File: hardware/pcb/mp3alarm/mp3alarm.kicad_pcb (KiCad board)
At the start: 2 copper layers, 68.6 x 47 mm, 18 parts, among them J1 AUDIO, J2 SW0, J3 SW1, J4 SW2, J5 I2C, J6 TM1637, J7 microSD, J9 ANT, U1 UDA1334A_Breakout, U2 mini_esp32, U3 RDA5807

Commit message: Updated PCB (added QR code, OSHW logo, etc) Some bugfixes for webinterface Updated README
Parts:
- added G***: LOGO, qr-code:qr-code, B.Cu at (98.8, 95.5)
- added G***: LOGO, qr-code:oshw, B.Cu at (99.1, 75.9)
- added G***: LOGO, qr-code:oshw, F.Cu at (120.1, 79.2)
- added J8: 5V, Connector_PinHeader_2.54mm:PinHeader_1x02_P2.54mm_Vertical, F.Cu at (47.0, 71.6)
- added JTAG: debug, Connector_PinHeader_2.54mm:PinHeader_2x05_P2.54mm_Vertical_SMD, B.Cu at (65.5, 96.3)
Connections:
- U2 pad 13: Net-(U2-Pad13) -> TMS
- U2 pad 18: Net-(U2-Pad18) -> TCK
- U2 pad 28: RDA_L -> I2S_MUTE
- U2 pad 30: Net-(U2-Pad30) -> TDI
- U2 pad 36: I2S_MUTE -> Net-(U2-Pad36)
- U2 pad 37: Net-(U2-Pad37) -> TDO
- U2 pad 4: Net-(U2-Pad4) -> RDA_L
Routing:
- net 5V: track 59.1 -> 95.9 mm
- net TDI: track 0.00 -> 30.1 mm, vias 0 -> 1
- net RDA_L: track 25.8 -> 8.17 mm
- net SD_CMD: track 18.5 -> 34.7 mm, vias 1 -> 2
- net TDO: track 0.00 -> 15.1 mm, vias 0 -> 1
- net TMS: track 0.00 -> 11.6 mm
- net TCK: track 0.00 -> 10.1 mm
- net SD_CD: track 20.3 -> 28.8 mm, vias 1 -> 2
- net I2S_MUTE: track 34.8 -> 27.5 mm, vias 0 -> 2
- net VCC: track 88.1 -> 94.1 mm
- net GND: vias 6 -> 8
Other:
- board text added: "ESP32 alarm clock v0.3"
- board text added: "NC"
- board text added: "TCK"
- board text added: "TDI"
- board text added: "TDO"
- board text added: "TMS"
- board text added: "VCC"
- board text removed: "ESP32 alarm clock"

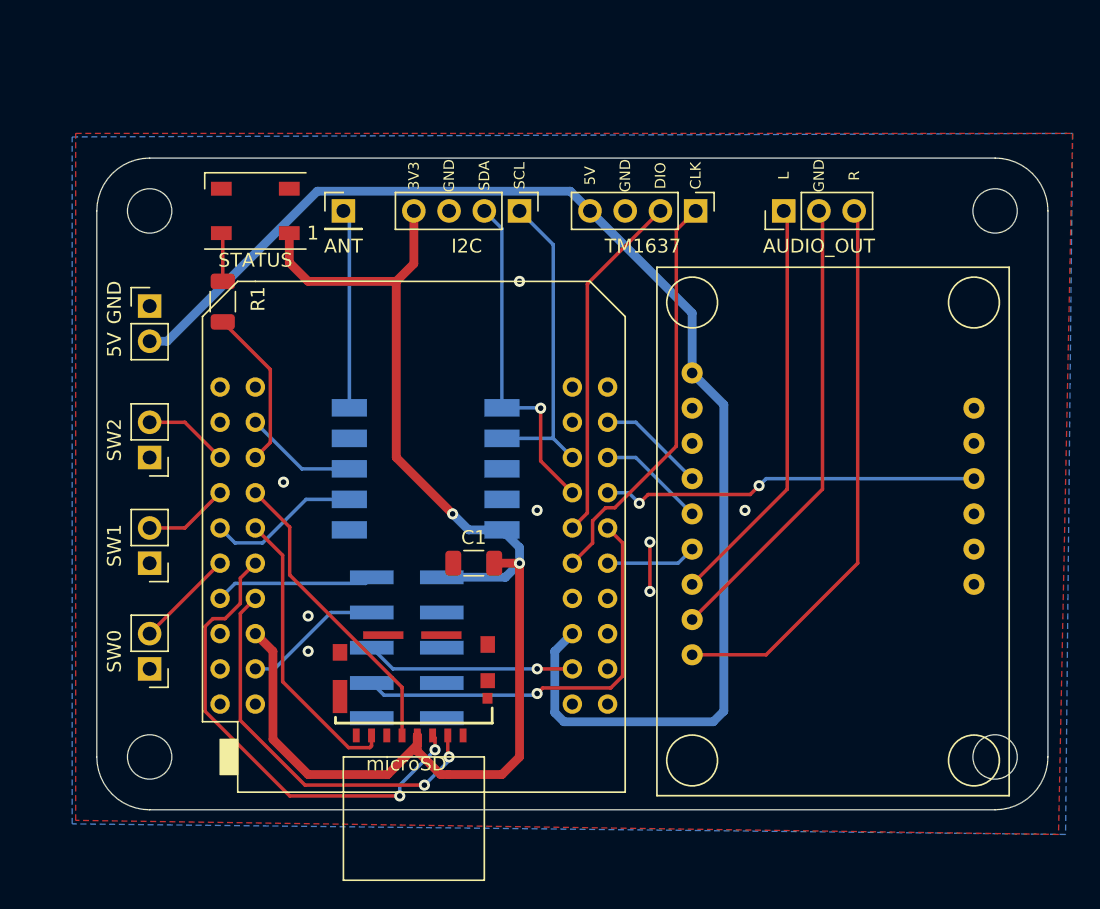
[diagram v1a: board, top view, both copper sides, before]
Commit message: New PCB with RDA5807FP
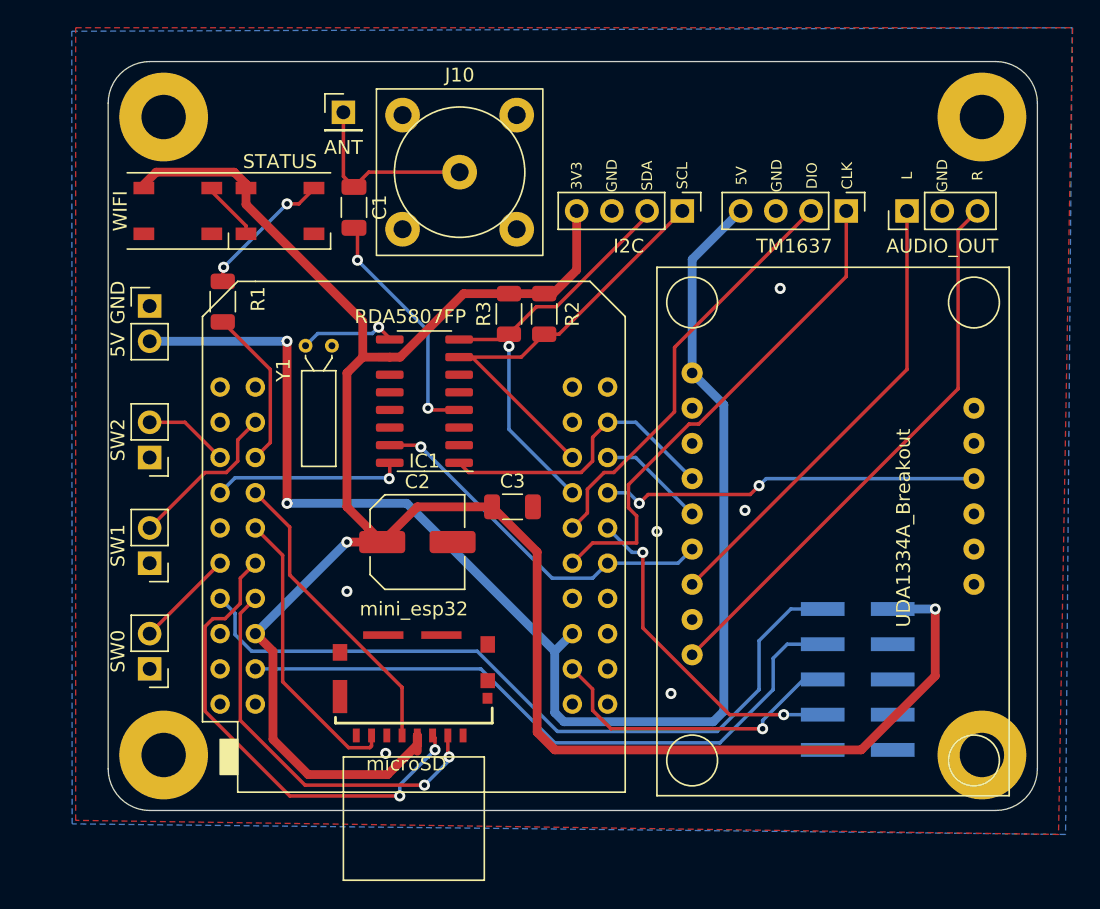
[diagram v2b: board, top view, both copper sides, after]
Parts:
- removed G***: LOGO, qr-code:qr-code
- removed G*** (x2): LOGO, qr-code:oshw
- removed JTAG: debug, Connector_PinHeader_2.54mm:PinHeader_2x05_P2.54mm_Vertical_SMD
- removed REF** (x4): MountingHole_3.2mm_M3, MountingHole:MountingHole_3.2mm_M3
- removed U3: RDA5807, pcb:RDA5807
- added C2: 10uF, Capacitor_SMD:C_Elec_6.3x5.4, F.Cu at (66.3, 88.6)
- added C3: 22nF, Capacitor_SMD:C_1206_3216Metric, F.Cu at (73.2, 86.1)
- added D2: WS2812B, LED_SMD:LED_WS2812B_PLCC4_5.0x5.0mm_P3.2mm, F.Cu at (49.0, 64.8)
- added H1: MountingHole_Pad, MountingHole:MountingHole_3.2mm_M3_Pad, F.Cu at (48.0, 58.0)
- added H2: MountingHole_Pad, MountingHole:MountingHole_3.2mm_M3_Pad, F.Cu at (48.0, 104.0)
- added H3: MountingHole_Pad, MountingHole:MountingHole_3.2mm_M3_Pad, F.Cu at (107.0, 104.0)
- added H4: MountingHole_Pad, MountingHole:MountingHole_3.2mm_M3_Pad, F.Cu at (107.0, 58.0)
- added IC1: RDA5807FP, Package_SO:SOP-16_3.9x9.9mm_P1.27mm, F.Cu at (66.8, 78.5)
- added J0: debug, Connector_PinHeader_2.54mm:PinHeader_2x05_P2.54mm_Vertical_SMD, B.Cu at (98.0, 98.6)
- added J10: Conn_Coaxial, Connector:F_Sat_Connector, F.Cu at (69.3, 62.0)
- added R2: 10k, Resistor_SMD:R_1206_3216Metric, F.Cu at (75.4, 72.2)
- added R3: 10k, Resistor_SMD:R_1206_3216Metric, F.Cu at (72.9, 72.2)
- added Y1: Crystal, Crystal:Crystal_C26-LF_D2.1mm_L6.5mm_Horizontal, F.Cu at (58.2, 74.5)
- C1: value C -> 1nF
- moved C1 27.1 mm to (61.7, 64.5), turned to -90 degrees
- moved J5 11.7 mm to (85.4, 64.8)
- moved J6 10.9 mm to (97.2, 64.8)
- moved J1 8.89 mm to (101.6, 64.8)
- moved J9 7.11 mm to (61.0, 57.7)
- moved D1 1.78 mm to (56.4, 64.8), turned to 0 degrees
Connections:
- C1 pad 1: GND -> ANT
- C1 pad 2: VCC -> Net-(C1-Pad2)
- J7 pad 1: Net-(J7-Pad1) -> unconnected-(J7-Pad1)
- J7 pad 8: Net-(J7-Pad8) -> unconnected-(J7-Pad8)
- J7 pad 9: Net-(J7-Pad9) -> unconnected-(J7-Pad9)
- U1 pad 10: Net-(U1-Pad10) -> unconnected-(U1-Pad10)
- U1 pad 11: Net-(U1-Pad11) -> unconnected-(U1-Pad11)
- U1 pad 13: Net-(U1-Pad13) -> unconnected-(U1-Pad13)
- U1 pad 14: Net-(U1-Pad14) -> unconnected-(U1-Pad14)
- U1 pad 15: Net-(U1-Pad15) -> unconnected-(U1-Pad15)
- U1 pad 2: Net-(U1-Pad2) -> unconnected-(U1-Pad2)
- U2 pad 15: Net-(U2-Pad15) -> unconnected-(U2-Pad15)
- U2 pad 17: Net-(U2-Pad17) -> unconnected-(U2-Pad17)
- U2 pad 19: Net-(U2-Pad19) -> unconnected-(U2-Pad19)
- U2 pad 2: Net-(U2-Pad2) -> unconnected-(U2-Pad2)
- U2 pad 20: Net-(U2-Pad20) -> unconnected-(U2-Pad20)
- U2 pad 21: Net-(U2-Pad21) -> unconnected-(U2-Pad21)
- U2 pad 23: Net-(U2-Pad23) -> unconnected-(U2-Pad23)
- U2 pad 3: Net-(U2-Pad3) -> unconnected-(U2-Pad3)
- U2 pad 34: Net-(U2-Pad34) -> unconnected-(U2-Pad34)
- U2 pad 36: Net-(U2-Pad36) -> unconnected-(U2-Pad36)
- U2 pad 38: Net-(U2-Pad38) -> unconnected-(U2-Pad38)
- U2 pad 39: Net-(U2-Pad39) -> unconnected-(U2-Pad39)
- U2 pad 4: RDA_L -> SW1
- U2 pad 40: Net-(U2-Pad40) -> unconnected-(U2-Pad40)
- U2 pad 7: SW1 -> I2S_RADIO_DOUT
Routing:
- net VCC: track 94.1 -> 161.7 mm
- net TMS: track 11.6 -> 54.0 mm
- net TCK: track 10.1 -> 47.4 mm
- net GND: track 36.9 -> 0.00 mm, vias 8 -> 6
- net I2S_BCLK: track 6.52 -> 26.6 mm, vias 0 -> 1
- net Net-(C1-Pad2): track 0.00 -> 17.5 mm, vias 0 -> 2
- net I2S_RADIO_DOUT: track 0.00 -> 13.8 mm, vias 0 -> 1
- net I2S_LRC: track 7.78 -> 21.3 mm
- net RDA_R: track 11.1 -> 0.00 mm
- net SCL: track 23.1 -> 31.6 mm
- net RDA_L: track 8.17 -> 0.00 mm
- net TDO: track 15.1 -> 22.6 mm
- net Net-(IC1-Pad9): track 0.00 -> 7.04 mm, vias 0 -> 1
- net 5V: track 95.9 -> 102.8 mm, vias 0 -> 2
- net TM_CLK: track 29.5 -> 36.3 mm
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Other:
- board size 68.6 x 47 mm -> 67 x 54 mm
- net class Default removed
- net class VCC removed
- board text added: "ESP32 alarm clock v0.4"
- board text added: "RDA5807FP"
- board text removed: "ESP32 alarm clock v0.3"
- board text removed: "RDA5807M"
- board text removed: "STATUS"

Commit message: * New partition table * Changed to audio pipeline (arduino-audio-tools) * PCB: new sat connector layout * PCB: added pullup resistors for switch pins
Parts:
- added R4: 10k, Resistor_SMD:R_1206_3216Metric, F.Cu at (49.5, 96.5)
- added R5: 10k, Resistor_SMD:R_1206_3216Metric, F.Cu at (49.5, 88.9)
- added R6: 10k, Resistor_SMD:R_1206_3216Metric, F.Cu at (49.5, 81.5)
- moved J2 0.51 mm to (46.5, 97.8)
- moved J3 0.51 mm to (46.5, 90.2)
- moved J4 0.51 mm to (46.5, 82.5)
- moved J8 0.51 mm to (46.5, 71.6)
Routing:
- net VCC: track 161.7 -> 189.9 mm, vias 2 -> 6
- net SW0: track 7.18 -> 9.21 mm
- net SW1: track 11.7 -> 13.0 mm
- net SW2: track 6.13 -> 6.75 mm
- net 5V: track 102.8 -> 103.3 mm

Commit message: PCB updates
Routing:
- net GND: vias 6 -> 8
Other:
- board text added: "ESP32 alarm clock v0.5"
- board text removed: "ESP32 alarm clock v0.4"

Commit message: * Latest PCB update for ESP32S3
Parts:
- removed J0: debug, Connector_PinHeader_2.54mm:PinHeader_2x05_P2.54mm_Vertical_SMD
- removed R4, R5: 10k, Resistor_SMD:R_1206_3216Metric
- removed U1: UDA1334A_Breakout, UDA1334A:UDA1334A-breakout
- added C10: 0.1uF, Capacitor_SMD:C_1206_3216Metric, F.Cu at (47.2, 86.1)
- added C11: 0.1uF, Capacitor_SMD:C_1206_3216Metric, F.Cu at (108.0, 74.7)
- added C12: 10uF, Capacitor_SMD:C_1206_3216Metric, F.Cu at (108.0, 77.2)
- added C13: 0.1uF, Capacitor_SMD:C_1206_3216Metric, F.Cu at (90.2, 75.2)
- added C14: 10uF, Capacitor_SMD:C_1206_3216Metric, F.Cu at (90.2, 72.6)
- added C15: 47uF, Capacitor_SMD:C_Elec_6.3x5.4, F.Cu at (99.6, 93.5)
- added C16: 47uF, Capacitor_SMD:C_Elec_6.3x5.4, F.Cu at (99.6, 100.8)
- added C17: 0.01uF, Capacitor_SMD:C_1206_3216Metric, F.Cu at (87.9, 87.9)
- added C18: 0.01uF, Capacitor_SMD:C_1206_3216Metric, F.Cu at (87.9, 90.4)
- added C19: 0.1uF, Capacitor_SMD:C_1206_3216Metric, F.Cu at (108.0, 82.3)
- added C20: 10uF, Capacitor_SMD:C_1206_3216Metric, F.Cu at (108.0, 79.8)
- added C21: 1nF, Capacitor_SMD:C_1206_3216Metric, F.Cu at (87.6, 64.8)
- added C4: 10uF, Capacitor_SMD:C_1206_3216Metric, F.Cu at (46.7, 98.6)
- added C5: 10uF, Capacitor_SMD:C_1206_3216Metric, F.Cu at (53.3, 90.2)
- added C6: 22uF, Capacitor_SMD:C_1206_3216Metric, F.Cu at (52.1, 86.1)
- added C7: 1uF, Capacitor_SMD:C_1206_3216Metric, F.Cu at (58.4, 87.4)
- added D3: D_Schottky, Diode_SMD:D_0805_2012Metric, F.Cu at (51.1, 98.6)
- added D4: PWR, LED_SMD:LED_0805_2012Metric, F.Cu at (65.0, 105.6)
- added FB1: FerriteBead_Small, Resistor_SMD:R_0805_2012Metric, F.Cu at (100.6, 77.5)
- added FB2: FerriteBead_Small, Resistor_SMD:R_0805_2012Metric, F.Cu at (100.6, 75.2)
- added J11: USB_C_Receptacle_USB2.0, Connector_USB:USB_C_Receptacle_JAE_DX07S016JA1R1500, F.Cu at (57.5, 105.3)
- added R10: 220k, Resistor_SMD:R_1206_3216Metric, F.Cu at (106.9, 93.5)
- added R11: 10k, Resistor_SMD:R_1206_3216Metric, F.Cu at (75.2, 95.5)
- added R12: 10k, Resistor_SMD:R_1206_3216Metric, F.Cu at (70.4, 95.5)
- added R13: 10k, Resistor_SMD:R_1206_3216Metric, F.Cu at (67.8, 95.5)
- added R14: 10k, Resistor_SMD:R_1206_3216Metric, F.Cu at (80.0, 95.5)
- added R15: 10k, Resistor_SMD:R_1206_3216Metric, F.Cu at (77.5, 95.5)
- added R16: 220k, Resistor_SMD:R_1206_3216Metric, F.Cu at (106.9, 98.0)
- added R17: 100, Resistor_SMD:R_1206_3216Metric, F.Cu at (92.7, 87.9)
- added R18: 100, Resistor_SMD:R_1206_3216Metric, F.Cu at (92.7, 90.4)
- added R19: 10k, Resistor_SMD:R_1206_3216Metric, F.Cu at (90.2, 80.3)
- added R20: 10k, Resistor_SMD:R_1206_3216Metric, F.Cu at (109.2, 86.6)
- added R21: 10k, Resistor_SMD:R_1206_3216Metric, F.Cu at (90.2, 82.8)
- added R22: 10k, Resistor_SMD:R_1206_3216Metric, F.Cu at (104.1, 86.6)
- added R23: 10k, Resistor_SMD:R_1206_3216Metric, F.Cu at (90.2, 77.7)
- added R24: 10k, Resistor_SMD:R_1206_3216Metric, F.Cu at (106.7, 86.6)
- added R7: 5k1, Resistor_SMD:R_1206_3216Metric, F.Cu at (60.7, 95.2)
- added R8: 10k, Resistor_SMD:R_1206_3216Metric, F.Cu at (55.9, 87.4)
- added R9: 680, Resistor_SMD:R_1206_3216Metric, F.Cu at (65.0, 101.0)
- added SW1: SW_RST, Button_Switch_SMD:SW_SPST_CK_RS282G05A3, F.Cu at (54.4, 59.4)
- added SW2: SW_BOOT, Button_Switch_SMD:SW_SPST_CK_RS282G05A3, F.Cu at (62.7, 59.4)
- added U3: ESP32-S3-WROOM-1, PCM_Espressif:ESP32-S3-WROOM-1, F.Cu at (54.0, 74.8)
- added U4: AMS1117-3.3, Package_TO_SOT_SMD:SOT-223-3_TabPin2, F.Cu at (48.0, 92.2)
- C2: value 10uF -> 1uF; footprint Capacitor_SMD:C_Elec_6.3x5.4 -> Capacitor_SMD:C_1206_3216Metric
- C3: value 22nF -> 10uF
- J4: value SW2 -> AudioJack3; footprint Connector_PinHeader_2.54mm:PinHeader_1x02_P2.54mm_Vertical -> footprints:PJ-313
- R6: value 10k -> 5k1
- U2: value mini_esp32 -> UDA1334ATS; footprint pcb:ESP32_mini -> Package_SO:SSOP-16_4.4x5.2mm_P0.65mm
- Y1: footprint Crystal:Crystal_C26-LF_D2.1mm_L6.5mm_Horizontal -> Crystal:Crystal_SMD_2012-2Pin_2.0x1.2mm
- moved J8 62.1 mm to (108.2, 64.8), turned to -90 degrees
- moved J4 49.1 mm to (90.9, 103.4), turned to -90 degrees
- moved J2 47.4 mm to (72.9, 58.4)
- moved J1 44.9 mm to (82.0, 105.2), turned to 180 degrees
- moved J3 39.0 mm to (69.1, 58.4)
- moved D2 37.8 mm to (79.5, 87.1), turned to 180 degrees
- moved U2 33.1 mm to (98.6, 82.5)
- moved J10 27.5 mm to (96.8, 60.7)
- moved J9 27.5 mm to (88.4, 56.4)
- moved D1 27.1 mm to (71.6, 87.1), turned to 180 degrees
- moved C2 26.7 mm to (66.0, 62.0), turned to -90 degrees
- moved C1 26.1 mm to (87.6, 67.3), turned to 0 degrees
- moved J6 22.3 mm to (76.8, 55.9), turned to 90 degrees
- moved R1 21.4 mm to (70.4, 82.8), turned to 0 degrees
- moved Y1 19.8 mm to (76.7, 67.3)
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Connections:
- C1 pad 2: Net-(C1-Pad2) -> Net-(J10-In)
- C2 pad 1: VCC -> GND
- C2 pad 2: GND -> BOOT
- C3 pad 1: VCC -> GND
- C3 pad 2: GND -> +5V
- D1 pad 1: VCC -> +5V
- D2 pad 1: VCC -> +5V
- IC1 pad 4: Net-(C1-Pad2) -> ANT
- J1 pad 1: Net-(J1-Pad1) -> OUT_L
- J1 pad 2: GND -> GNDA
- J1 pad 3: Net-(J1-Pad3) -> OUT_R
- J10 pad 1: ANT -> Net-(J10-In)
- J6 pad 4: 5V -> +5V
- J7 pad 1: unconnected-(J7-Pad1) -> SD_D2
- J7 pad 2: SD_CD -> SD_D3
- J7 pad 7: SD_DATA0 -> SD_D0
- J7 pad 8: unconnected-(J7-Pad8) -> SD_D1
- J8 pad 2: 5V -> +5V
- J9 pad 1: ANT -> Net-(J9-Pin_1)
- R6 pad 1: VCC -> GND
- R6 pad 2: SW2 -> Net-(J11-CC1)
- U2 pad 1: GND -> I2S_BCLK
- U2 pad 10: SD_DATA0 -> Net-(U2-PLL0)
- U2 pad 11: SW0 -> Net-(U2-SFOR0)
- U2 pad 12: SD_CMD -> Net-(U2-Vref(DAC))
- U2 pad 13: TMS -> Net-(U2-VDDA)
- U2 pad 14: SD_CD -> Net-(U2-VOUTL)
- U2 pad 15: unconnected-(U2-Pad15) -> GNDA
- U2 pad 16: VCC -> Net-(U2-VOUTR)
- U2 pad 2: unconnected-(U2-Pad2) -> I2S_LRC
- U2 pad 3: unconnected-(U2-Pad3) -> I2S_DIN
- U2 pad 4: SW1 -> VCC
- U2 pad 5: SW2 -> GND
- U2 pad 6: STATUS_DATA -> Net-(U2-SYSCLK/PLL1)
- U2 pad 7: I2S_RADIO_DOUT -> Net-(U2-SFOR1)
- U2 pad 8: SD_CLK -> I2S_MUTE
- U2 pad 9: RDA_R -> I2S_DEEM
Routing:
- net +5V: track 0.00 -> 107.7 mm, vias 0 -> 2
- net 5V: track 103.3 -> 0.00 mm, vias 2 -> 0
- net TMS: track 54.0 -> 0.00 mm
- net I2S_DIN: track 7.78 -> 58.8 mm, vias 0 -> 4
- net SD_D2: track 0.00 -> 47.5 mm, vias 0 -> 2
- net TCK: track 47.4 -> 0.00 mm
- net SD_D3: track 0.00 -> 45.0 mm, vias 0 -> 2
- net I2S_DEEM: track 0.00 -> 43.5 mm, vias 0 -> 2
- net Net-(J1-Pad3): track 40.5 -> 0.00 mm
- net I2S_LRC: track 21.3 -> 61.5 mm, vias 0 -> 4
- net SD_D0: track 0.00 -> 38.2 mm, vias 0 -> 2
- net Net-(U3-EN): track 0.00 -> 38.1 mm, vias 0 -> 3
- net SD_D1: track 0.00 -> 36.5 mm, vias 0 -> 2
- net Net-(J1-Pad1): track 33.3 -> 0.00 mm
- net OUT_L: track 0.00 -> 33.2 mm
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- added copper zone on B.Cu, net GNDA
- added copper zone on F.Cu, net GNDA
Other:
- board text added: "ESP32 alarm clock v0.7"
- board text added: "TM1637↑"
- board text removed: "ESP32 alarm clock v0.5"
- board text removed: "NC"
- board text removed: "SW2"
- board text removed: "TCK"
- board text removed: "TDI"
- board text removed: "TDO"
- board text removed: "TM1637"
- board text removed: "TMS"
- board text removed: "VCC"
